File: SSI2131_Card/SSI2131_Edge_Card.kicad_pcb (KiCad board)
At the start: 2 copper layers, 62 parts, among them Q1 2N3906, Q2 2N3906, U1 CD4066BM, U2 OPA1678, U3 OPA1678, U4 LM13700, U5 SSI2131, U6 SSI2131, U7 LM4040DBZ-2.5

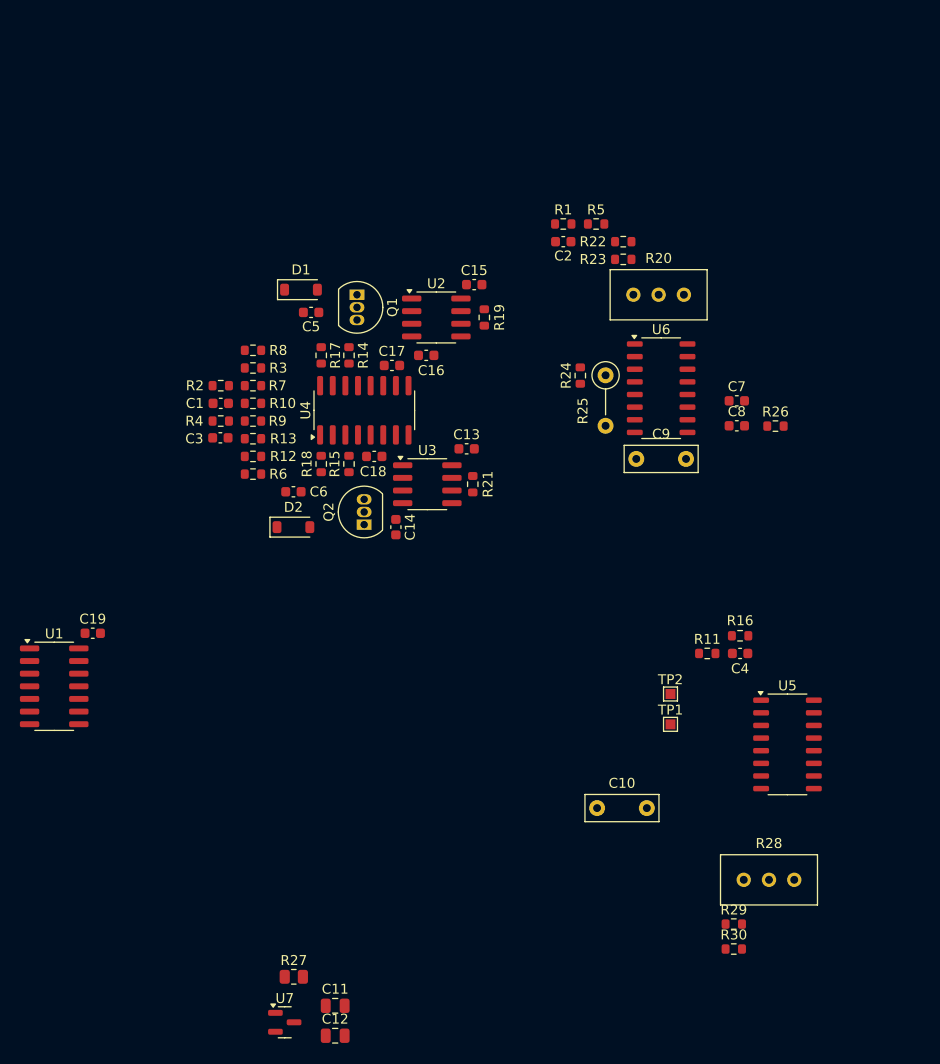
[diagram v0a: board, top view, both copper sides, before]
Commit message: Aded Heiarchy in Kicad, adjusted overall VCA design
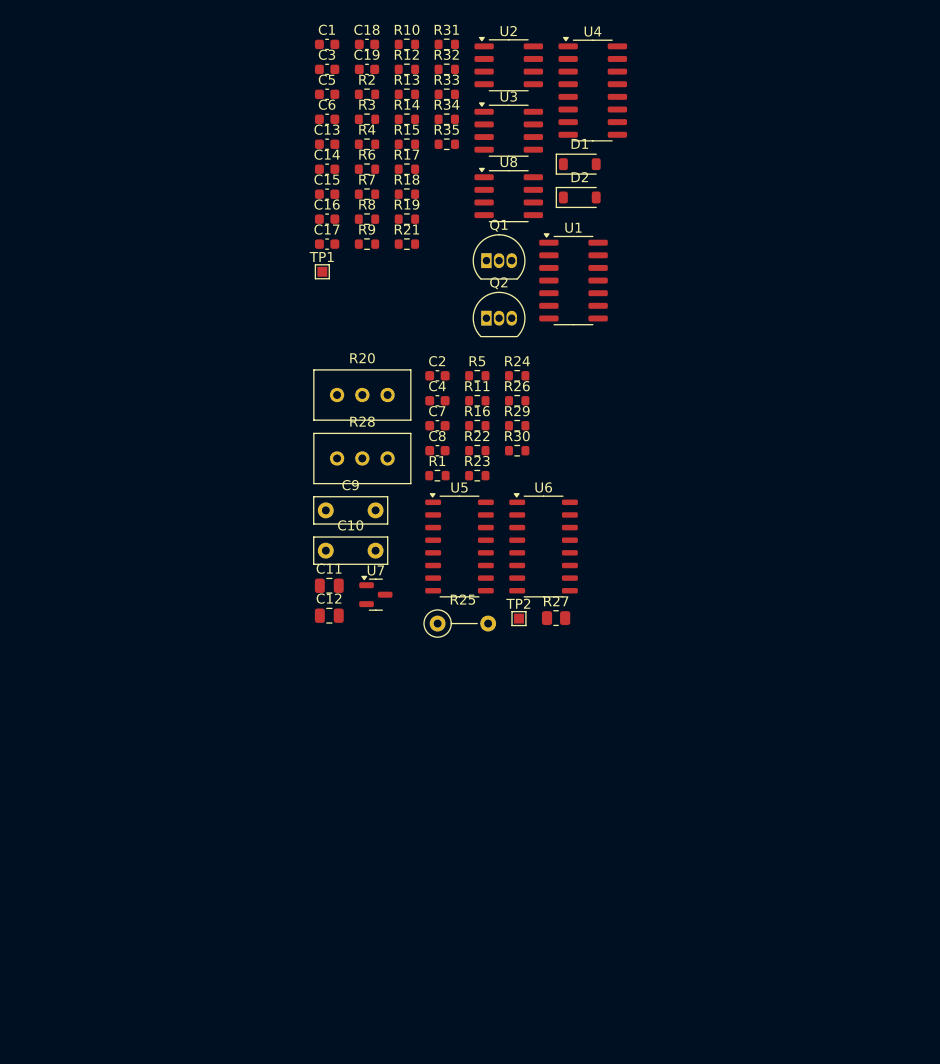
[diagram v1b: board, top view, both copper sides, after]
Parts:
- added R31: 1k, Resistor_SMD:R_0603_1608Metric, F.Cu at (126.8, 63.7)
- added R32: 1k, Resistor_SMD:R_0603_1608Metric, F.Cu at (126.8, 66.2)
- added R33: 1k, Resistor_SMD:R_0603_1608Metric, F.Cu at (126.8, 68.8)
- added R34: 1k, Resistor_SMD:R_0603_1608Metric, F.Cu at (126.8, 71.3)
- added R35: 1k, Resistor_SMD:R_0603_1608Metric, F.Cu at (126.8, 73.8)
- added U8: OPA1678, Package_SO:SOIC-8_3.9x4.9mm_P1.27mm, F.Cu at (133.0, 79.0)
- TP1: value 2V5 TP -> PMOD_TP
- moved U1 66.3 mm to (139.5, 87.5)
- moved C19 63.0 mm to (118.8, 66.2)
- moved R28 58.9 mm to (120.8, 105.4)
- moved TP1 57.4 mm to (114.3, 86.6)
- moved R30 54.6 mm to (133.9, 104.6)
- moved R29 54.6 mm to (133.9, 102.1)
- moved R27 44.7 mm to (137.8, 121.4)
- moved U7 44.0 mm to (119.7, 119.1)
- moved D2 43.9 mm to (140.2, 79.1)
- moved C11 42.2 mm to (115.0, 118.2)
- moved C12 42.2 mm to (115.0, 121.2)
- moved R12 41.9 mm to (122.8, 66.2)
- moved C18 41.4 mm to (118.8, 63.7), turned to 0 degrees
- moved C4 39.6 mm to (125.8, 99.6)
- moved U4 39.5 mm to (141.5, 68.4), turned to 0 degrees
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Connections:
- net /PMOD_A_AMT renamed /Pitch and PWM modulation/PMOD_AMT
- net /PMOD_A_EN renamed /Pitch and PWM modulation/PMOD_EN
- net /PMOD_A_IN renamed /Pitch and PWM modulation/PMOD_IN
- net /PMOD_B_AMT renamed /Pitch and PWM modulation/PMOD_B_AMT
- net /PMOD_B_EN renamed /Pitch and PWM modulation/PMOD_B_EN
- net /PMOD_B_IN renamed /Pitch and PWM modulation/PMOD_B_IN
- R19 pad 2: /A_EXPO_IN -> /Pitch and PWM modulation/PMOD_SCALED
- R21 pad 2: /B_EXPO_IN -> Net-(R21-Pad2)
- TP1 pad 1: /A_EXPO_IN -> /Pitch and PWM modulation/PMOD_SCALED
- U2 pad 7: /A_EXPO_IN -> /Pitch and PWM modulation/PMOD_SCALED
- U3 pad 7: /B_EXPO_IN -> Net-(R21-Pad2)

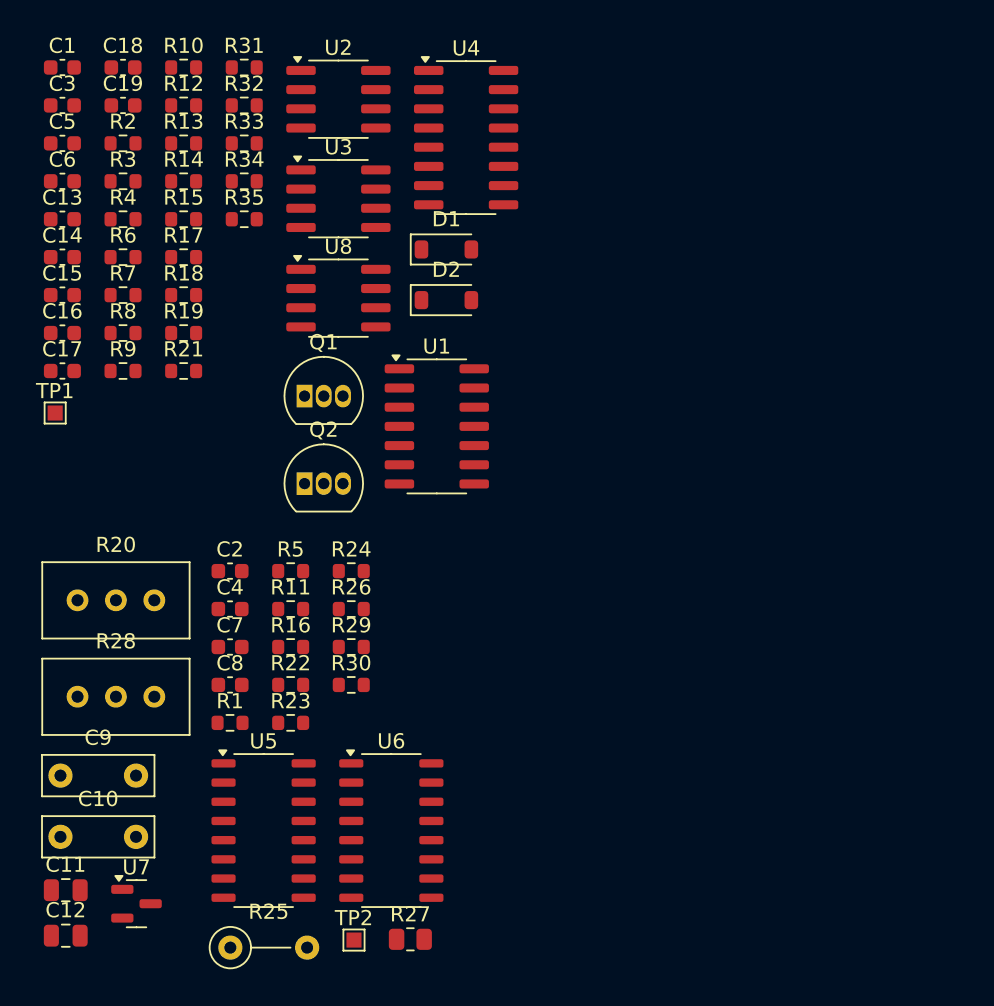
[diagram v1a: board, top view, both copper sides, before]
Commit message: Added pin lables and added VCOs into their own heiarchy sheets
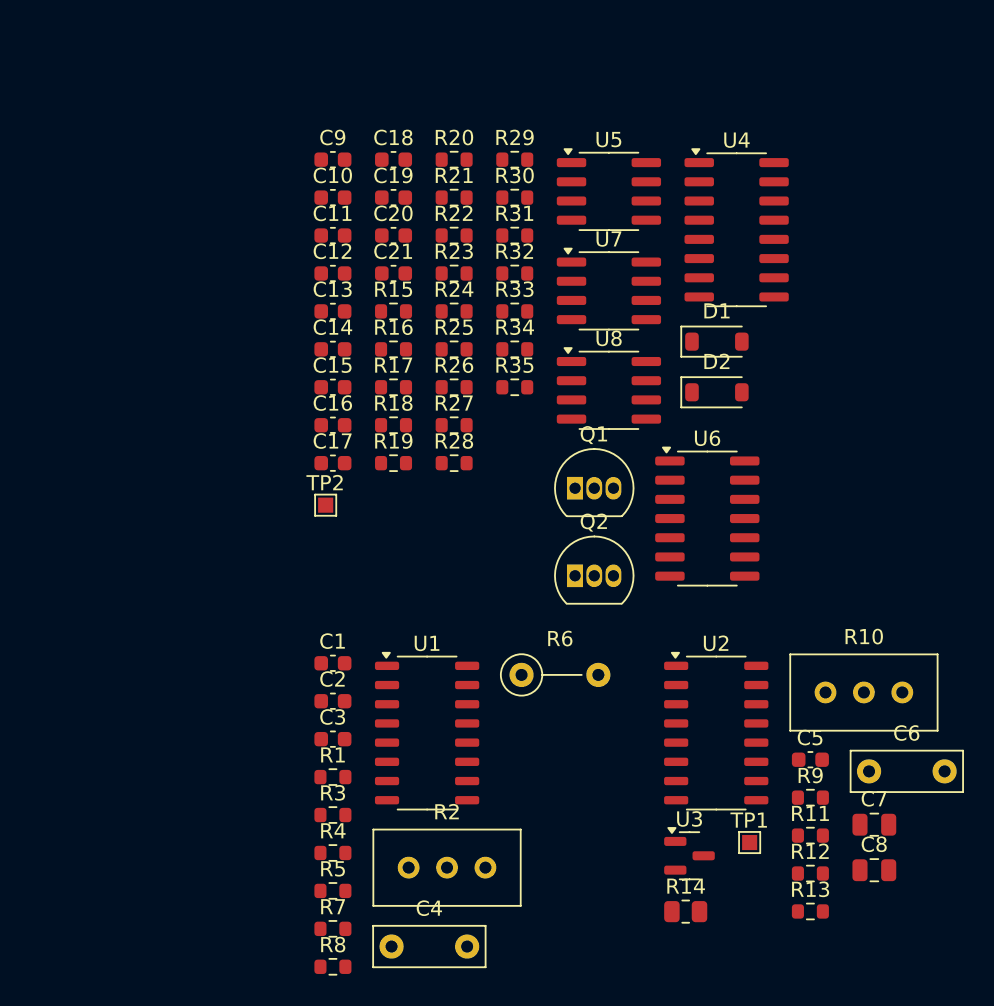
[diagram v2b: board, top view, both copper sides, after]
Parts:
- added C20: 0.1uf, Capacitor_SMD:C_0603_1608Metric, F.Cu at (136.7, 74.8)
- added C21: 0.1uf, Capacitor_SMD:C_0603_1608Metric, F.Cu at (136.7, 77.4)
- C1: value 470nF -> 220nF
- C10: value 3.9nf -> 470nF; footprint Capacitor_THT:C_Rect_L7.2mm_W2.5mm_P5.00mm_FKS2_FKP2_MKS2_MKP2 -> Capacitor_SMD:C_0603_1608Metric
- C11, C12: value 1uf -> 0.1uf; footprint Capacitor_SMD:C_0805_2012Metric -> Capacitor_SMD:C_0603_1608Metric
- C18: value 0.1uf -> 1nF
- C19: value 0.1uf -> 470nF
- C2: value 220nF -> 10n
- C3: value 470nF -> 10n
- C4: value 220nF -> 3.9nf; footprint Capacitor_SMD:C_0603_1608Metric -> Capacitor_THT:C_Rect_L7.2mm_W2.5mm_P5.00mm_FKS2_FKP2_MKS2_MKP2
- C5: value 1nF -> 220nF
- C6: value 1nF -> 3.9nf; footprint Capacitor_SMD:C_0603_1608Metric -> Capacitor_THT:C_Rect_L7.2mm_W2.5mm_P5.00mm_FKS2_FKP2_MKS2_MKP2
- C7, C8: value 10n -> 1uf; footprint Capacitor_SMD:C_0603_1608Metric -> Capacitor_SMD:C_0805_2012Metric
- C9: value 3.9nf -> 1nF; footprint Capacitor_THT:C_Rect_L7.2mm_W2.5mm_P5.00mm_FKS2_FKP2_MKS2_MKP2 -> Capacitor_SMD:C_0603_1608Metric
- R1: value 680 -> 100k
- R10: value 1k -> 5k; footprint Resistor_SMD:R_0603_1608Metric -> Potentiometer_THT:Potentiometer_Bourns_3296W_Vertical
- R11: value 680 -> 10k
- R12: value 2.5k -> 680
- R13: value 1k -> 20k
- R14: value 1k -> 2k; footprint Resistor_SMD:R_0603_1608Metric -> Resistor_SMD:R_0805_2012Metric
- R15: value 1k -> 10k
- R16: value 20k -> 2.5k
- R18: value 6.8k -> 33k
- R19: value 33k -> 120k
- R2: value 120k -> 5k; footprint Resistor_SMD:R_0603_1608Metric -> Potentiometer_THT:Potentiometer_Bourns_3296W_Vertical
- R20: value 5k -> 3.9k; footprint Potentiometer_THT:Potentiometer_Bourns_3296W_Vertical -> Resistor_SMD:R_0603_1608Metric
- R21: value 33k -> 1k
- R22: value 10k -> 1k
- R23: value 100k -> 10k
- R24: value 4.3k -> 2.5k
- R25: value 267k -> 1k; footprint Resistor_THT:R_Axial_DIN0207_L6.3mm_D2.5mm_P5.08mm_Vertical -> Resistor_SMD:R_0603_1608Metric
- R26: value 10k -> 6.8k
- R27: value 2k -> 1k; footprint Resistor_SMD:R_0805_2012Metric -> Resistor_SMD:R_0603_1608Metric
- R28: value 5k -> 1k; footprint Potentiometer_THT:Potentiometer_Bourns_3296W_Vertical -> Resistor_SMD:R_0603_1608Metric
- R29: value 10k -> 33k
- R30: value 100k -> 120k
- R31: value 1k -> 3.9k
- R4: value 120k -> 680
- R6: value 10k -> 267k; footprint Resistor_SMD:R_0603_1608Metric -> Resistor_THT:R_Axial_DIN0207_L6.3mm_D2.5mm_P5.08mm_Vertical
- R7: value 3.9k -> 4.3k
- R8: value 2.5k -> 10k
- R9: value 3.9k -> 100k
- TP1: value PMOD_TP -> 2V5 TP
- TP2: value 2V5 TP -> PMOD_TP
- U1: value CD4066BM -> SSI2131; footprint Package_SO:SOIC-14_3.9x8.7mm_P1.27mm -> Package_SO:STC_SOP-16_3.9x9.9mm_P1.27mm
- U2: value OPA1678 -> SSI2131; footprint Package_SO:SOIC-8_3.9x4.9mm_P1.27mm -> Package_SO:STC_SOP-16_3.9x9.9mm_P1.27mm
- U3: value OPA1678 -> LM4040DBZ-2.5; footprint Package_SO:SOIC-8_3.9x4.9mm_P1.27mm -> Package_TO_SOT_SMD:SOT-23
- U5: value SSI2131 -> OPA1678; footprint Package_SO:STC_SOP-16_3.9x9.9mm_P1.27mm -> Package_SO:SOIC-8_3.9x4.9mm_P1.27mm
- U6: value SSI2131 -> CD4066BM; footprint Package_SO:STC_SOP-16_3.9x9.9mm_P1.27mm -> Package_SO:SOIC-14_3.9x8.7mm_P1.27mm
- U7: value LM4040DBZ-2.5 -> OPA1678; footprint Package_TO_SOT_SMD:SOT-23 -> Package_SO:SOIC-8_3.9x4.9mm_P1.27mm
- moved C6 66.1 mm to (168.1, 110.3)
- moved R12 65.6 mm to (164.2, 117.1)
- moved R13 65.6 mm to (164.2, 119.6)
- moved C5 64.1 mm to (164.2, 109.5)
- moved R10 63.0 mm to (170.3, 105.1)
- moved R14 58.6 mm to (156.0, 119.6)
- moved TP1 54.0 mm to (160.2, 115.0)
- moved R2 53.6 mm to (142.7, 116.7)
- moved R9 53.5 mm to (164.2, 112.0)
- moved U7 51.2 mm to (150.9, 78.5)
- moved U3 49.3 mm to (156.2, 115.9)
- moved U2 48.8 mm to (158.0, 107.8)
- moved U5 48.1 mm to (150.9, 71.9)
- moved C12 47.2 mm to (132.6, 77.4)
- moved C11 46.8 mm to (132.6, 74.8)
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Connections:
- net /Pitch and PWM modulation/PMOD_B_IN renamed /OSC A/A_Tri
- C1 pad 2: Net-(C1-Pad2) -> GND
- C10 pad 1: unconnected-(C10-Pad1) -> Net-(C10-Pad1)
- C10 pad 2: unconnected-(C10-Pad2) -> Net-(C10-Pad2)
- C11 pad 1: +2V5 -> +5V
- C12 pad 1: +2V5 -> +5V
- C14 pad 1: -12V -> +5V
- C15 pad 1: +5V -> -12V
- C17 pad 1: +5V -> -12V
- C18 pad 1: -12V -> Net-(D2-K)
- C18 pad 2: GND -> Net-(D2-A)
- C19 pad 1: +5V -> Net-(C19-Pad1)
- C19 pad 2: GND -> Net-(C19-Pad2)
- C2 pad 1: Net-(C2-Pad1) -> unconnected-(C2-Pad1)
- C2 pad 2: GND -> Net-(U1-SOFT_SYNC)
- C3 pad 1: Net-(C3-Pad1) -> unconnected-(C3-Pad1)
- C3 pad 2: Net-(C3-Pad2) -> Net-(U1-HARD_SYNC)
- C4 pad 1: Net-(C4-Pad1) -> Net-(U1-TCAP)
- C5 pad 1: Net-(D1-K) -> Net-(C5-Pad1)
- C5 pad 2: Net-(D1-A) -> GND
- C6 pad 1: Net-(D2-K) -> unconnected-(C6-Pad1)
- C6 pad 2: Net-(D2-A) -> unconnected-(C6-Pad2)
- C7 pad 1: unconnected-(C7-Pad1) -> +2V5
- C7 pad 2: Net-(U6-SOFT_SYNC) -> GND
- C8 pad 1: unconnected-(C8-Pad1) -> +2V5
- C8 pad 2: Net-(U6-HARD_SYNC) -> GND
- C9 pad 1: Net-(U6-TCAP) -> Net-(D1-K)
- C9 pad 2: GND -> Net-(D1-A)
- R1 pad 1: /Pitch_CV_A -> /OSC A/A_EXPO_IN
- R1 pad 2: Net-(C2-Pad1) -> +2V5
- R10 pad 1: GND -> +2V5
- R10 pad 2: Net-(U4A--) -> Net-(R10-Pad2)
- R11 pad 1: /Pitch_CV_B -> Net-(R10-Pad2)
- R11 pad 2: Net-(C4-Pad1) -> /B_EXPO_IN
- R12 pad 1: Net-(D2-K) -> /Pitch_CV_B
- R12 pad 2: Net-(R12-Pad2) -> Net-(C5-Pad1)
- R13 pad 1: GND -> Net-(C5-Pad1)
- R13 pad 2: Net-(U4C--) -> /B_EXPO_IN
- R14 pad 1: GND -> +5V
- R14 pad 2: Net-(U4A-+) -> +2V5
- R15 pad 1: GND -> Net-(R15-Pad1)
- R15 pad 2: Net-(U4C-+) -> /Pitch and PWM modulation/PMOD_AMT
- R16 pad 1: Net-(C4-Pad1) -> Net-(D1-K)
- R16 pad 2: /B_EXPO_IN -> Net-(R15-Pad1)
- R18 pad 1: Net-(Q2-C) -> Net-(U5B--)
- R18 pad 2: Net-(R18-Pad2) -> /OSC A/A_EXPO_IN
- R19 pad 1: Net-(U2B--) -> Net-(C10-Pad2)
- R19 pad 2: /Pitch and PWM modulation/PMOD_SCALED -> Net-(R19-Pad2)
- R2 pad 1: Net-(C1-Pad2) -> +2V5
- R20 pad 1: +2V5 -> Net-(R19-Pad2)
- R20 pad 2: Net-(R20-Pad2) -> Net-(U4A--)
- R21 pad 1: Net-(U3B--) -> GND
- R21 pad 2: Net-(R21-Pad2) -> Net-(U4A--)
- R22 pad 1: Net-(R20-Pad2) -> GND
- R22 pad 2: /A_EXPO_IN -> Net-(U4A-+)
- R23 pad 1: /A_EXPO_IN -> Net-(R23-Pad1)
- R23 pad 2: +2V5 -> /Pitch and PWM modulation/PWM_MOD_AMOUNT
- R24 pad 1: GND -> Net-(D2-K)
- R24 pad 2: Net-(U6-HF_TRACK) -> Net-(R23-Pad1)
- R25 pad 1: Net-(U6-HF_TRACK) -> /Pitch and PWM modulation/2.5V_REF
- R25 pad 2: /A_EXPO_IN -> Net-(U8B--)
- R26 pad 1: GND -> Net-(Q2-C)
- R26 pad 2: Net-(U6-HARD_SYNC) -> Net-(R26-Pad2)
- R27 pad 1: +5V -> Net-(U8A--)
- R27 pad 2: +2V5 -> /OSC A/PWM_MOD_IN
- R28 pad 1: +2V5 -> Net-(U8B--)
- R29 pad 1: Net-(R28-Pad2) -> Net-(U7B--)
- R29 pad 2: /B_EXPO_IN -> Net-(R29-Pad2)
- R3 pad 1: Net-(R3-Pad1) -> Net-(R2-Pad2)
- R3 pad 2: /Pitch and PWM modulation/PMOD_AMT -> /OSC A/A_EXPO_IN
- R30 pad 1: /B_EXPO_IN -> Net-(C19-Pad2)
- R30 pad 2: +2V5 -> Net-(R30-Pad2)
- R31 pad 1: Net-(U8B--) -> Net-(R30-Pad2)
- R31 pad 2: Net-(R21-Pad2) -> Net-(U4C--)
- R32 pad 1: /Pitch and PWM modulation/2.5V_REF -> Net-(R28-Pad2)
- R32 pad 2: Net-(U8B--) -> Net-(U8A--)
- R33 pad 2: Net-(R33-Pad2) -> Net-(R29-Pad2)
- R34 pad 1: Net-(R33-Pad2) -> GND
- R34 pad 2: Net-(U8A--) -> Net-(U4C--)
- R35 pad 1: Net-(U8A--) -> GND
- R35 pad 2: /Pitch and PWM modulation/PWM_MOD_OUT -> Net-(U4C-+)
- R4 pad 1: Net-(C3-Pad2) -> unconnected-(R4-Pad1)
- R4 pad 2: Net-(R4-Pad2) -> Net-(C1-Pad1)
- R5 pad 1: Net-(C2-Pad1) -> Net-(C1-Pad1)
- R5 pad 2: /A_EXPO_IN -> unconnected-(R5-Pad2)
- R6 pad 1: Net-(R12-Pad2) -> Net-(U1-HF_TRACK)
- R6 pad 2: /Pitch and PWM modulation/PMOD_B_AMT -> /OSC A/A_EXPO_IN
- R7 pad 1: Net-(R2-Pad2) -> GND
- R7 pad 2: Net-(U4A--) -> Net-(U1-HF_TRACK)
- R8 pad 1: Net-(D1-K) -> GND
- R8 pad 2: Net-(R3-Pad1) -> Net-(U1-HARD_SYNC)
- R9 pad 1: Net-(R4-Pad2) -> /B_EXPO_IN
- R9 pad 2: Net-(U4C--) -> +2V5
- TP1 pad 1: /Pitch and PWM modulation/PMOD_SCALED -> +2V5
- TP2 pad 1: +2V5 -> /OSC A/A_EXPO_IN
- U1 pad 1: /Pitch and PWM modulation/PMOD_IN -> /OSC A/A_Saw
- U1 pad 10: unconnected-(U1-Pad10) -> Net-(U1-HARD_SYNC)
- U1 pad 11: unconnected-(U1-Pad11) -> Net-(U1-SOFT_SYNC)
- U1 pad 13: /Pitch and PWM modulation/PMOD_EN -> unconnected-(U1-EXPO_SCALE-Pad13)
- U1 pad 14: +5V -> unconnected-(U1-VREF-Pad14)
- U1 pad 2: Net-(C1-Pad1) -> /OSC A/A_Pulse
- U1 pad 3: Net-(C3-Pad1) -> unconnected-(U1-PWM_CTRL-Pad3)
- U1 pad 5: /Pitch and PWM modulation/PMOD_B_EN -> Net-(U1-HF_TRACK)
- U1 pad 6: unconnected-(U1-Pad6) -> /OSC A/A_EXPO_IN
- U1 pad 7: GND -> unconnected-(U1-V--Pad7)
- U1 pad 8: unconnected-(U1-Pad8) -> Net-(U1-TCAP)
- U2 pad 1: Net-(Q1-B) -> unconnected-(U2-SAW_OUT-Pad1)
- U2 pad 2: Net-(D1-K) -> unconnected-(U2-PULSE_OUT-Pad2)
- U2 pad 3: GND -> unconnected-(U2-PWM_CTRL-Pad3)
- U2 pad 4: -12V -> unconnected-(U2-TRI_OUT-Pad4)
- U2 pad 5: GND -> unconnected-(U2-HF_TRACK-Pad5)
- U2 pad 6: Net-(U2B--) -> /B_EXPO_IN
- U2 pad 7: /Pitch and PWM modulation/PMOD_SCALED -> unconnected-(U2-V--Pad7)
- U2 pad 8: +5V -> unconnected-(U2-TCAP-Pad8)
- U3 pad 1: Net-(Q2-B) -> +2V5
- U3 pad 2: Net-(D2-K) -> GND
- U3 pad 3: GND -> unconnected-(U3-NC-Pad3)
- U4 pad 1: Net-(R18-Pad2) -> Net-(R26-Pad2)
- U4 pad 12: Net-(U2B--) -> Net-(U5B--)
- U4 pad 5: Net-(U3B--) -> Net-(U7B--)
- U5 pad 1: unconnected-(U5-SAW_OUT-Pad1) -> Net-(Q1-B)
- U5 pad 2: unconnected-(U5-PULSE_OUT-Pad2) -> Net-(D1-K)
- U5 pad 3: unconnected-(U5-PWM_CTRL-Pad3) -> GND
- U5 pad 4: unconnected-(U5-TRI_OUT-Pad4) -> -12V
- U5 pad 5: unconnected-(U5-HF_TRACK-Pad5) -> GND
- U5 pad 6: /B_EXPO_IN -> Net-(U5B--)
- U5 pad 7: unconnected-(U5-V--Pad7) -> /OSC A/A_EXPO_IN
- U5 pad 8: unconnected-(U5-TCAP-Pad8) -> +5V
- U6 pad 1: unconnected-(U6-SAW_OUT-Pad1) -> /Pitch and PWM modulation/PMOD_IN
- U6 pad 10: Net-(U6-HARD_SYNC) -> unconnected-(U6-Pad10)
- U6 pad 11: Net-(U6-SOFT_SYNC) -> unconnected-(U6-Pad11)
- U6 pad 13: unconnected-(U6-EXPO_SCALE-Pad13) -> /Pitch and PWM modulation/PMOD_EN
- U6 pad 14: unconnected-(U6-VREF-Pad14) -> +5V
- U6 pad 2: unconnected-(U6-PULSE_OUT-Pad2) -> Net-(C10-Pad1)
- U6 pad 3: unconnected-(U6-PWM_CTRL-Pad3) -> Net-(C19-Pad1)
- U6 pad 4: unconnected-(U6-TRI_OUT-Pad4) -> /Pitch and PWM modulation/PWM_MOD_IN
- U6 pad 5: Net-(U6-HF_TRACK) -> /Pitch and PWM modulation/PWM_MOD_EN
- U6 pad 6: /A_EXPO_IN -> unconnected-(U6-Pad6)
- U6 pad 7: unconnected-(U6-V--Pad7) -> GND
- U6 pad 8: Net-(U6-TCAP) -> unconnected-(U6-Pad8)
- U7 pad 1: +2V5 -> Net-(Q2-B)
- U7 pad 2: GND -> Net-(D2-K)
- U7 pad 3: unconnected-(U7-NC-Pad3) -> GND
- U8 pad 1: /Pitch and PWM modulation/PWM_MOD_OUT -> /OSC A/PWM_MOD_IN
- U8 pad 4: unconnected-(U8C-V--Pad4) -> -12V
- U8 pad 7: Net-(R33-Pad2) -> Net-(R28-Pad2)
- U8 pad 8: unconnected-(U8C-V+-Pad8) -> +5V
